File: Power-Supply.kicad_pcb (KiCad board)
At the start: 2 copper layers, 76 x 76.2 mm, 72 parts, among them J2 ADC1, J3 ADC2, J4 DAC1, J5 DAC2, J6 DAC3, J7 FPGA, J8 Frontpanel, J9 RPT-75C, U1 LT3081xR, U2 LT3081xR, U3 LT3091xR, U4 SIP10-05, U5 AMS1117-3.3, U6 DNT04

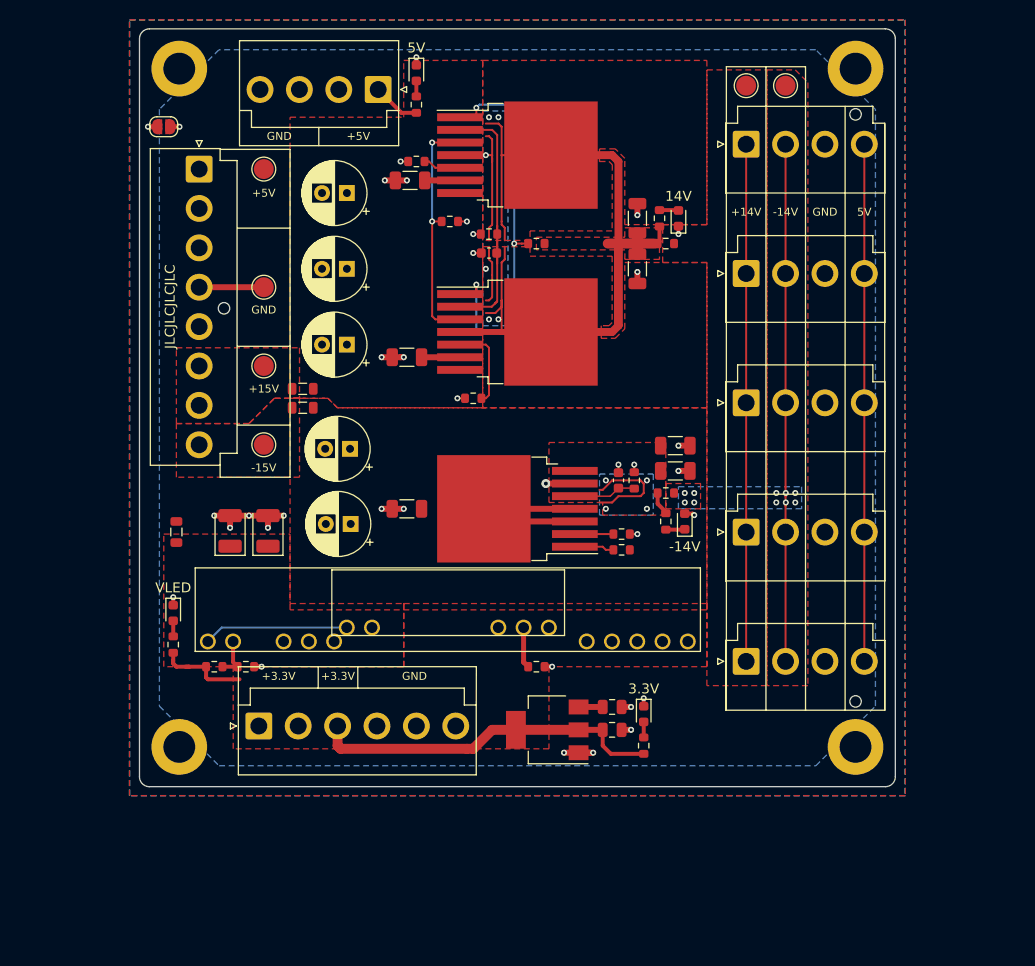
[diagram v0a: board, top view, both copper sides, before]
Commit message: Update to KiCad 6
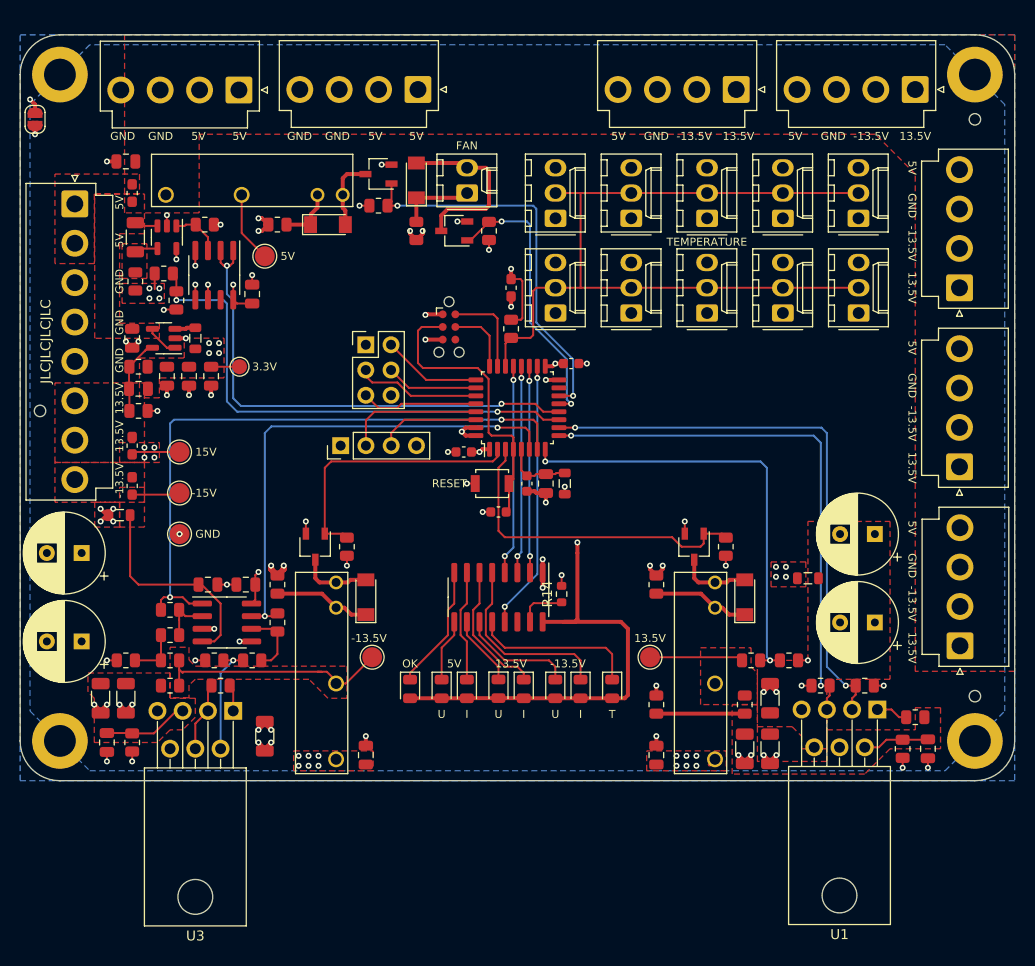
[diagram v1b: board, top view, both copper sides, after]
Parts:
- removed C10, C9: 10u, Capacitor_SMD:C_0805_2012Metric
- removed C11, C12: 100u, Capacitor_Tantalum_SMD:CP_EIA-3528-21_Kemet-B
- removed C13: 10u/50V, Capacitor_SMD:C_1206_3216Metric
- removed C18: 220u, Capacitor_THT:CP_Radial_D6.3mm_P2.50mm
- removed L1: 600R/100M, Inductor_SMD:L_0805_2012Metric
- removed R19, R20: NC, Resistor_SMD:R_0603_1608Metric
- removed R21: 3k, Resistor_SMD:R_0603_1608Metric
- removed U5: AMS1117-3.3, Package_TO_SOT_SMD:SOT-223-3_TabPin2
- removed U6: DNT04, twam-Misc:DNT04
- added C19: 100nF, Capacitor_SMD:C_0805_2012Metric, F.Cu at (164.0, 134.9)
- added C20: 100nF, Capacitor_SMD:C_0805_2012Metric, F.Cu at (134.8, 134.9)
- added C21: 100nF, Capacitor_SMD:C_0805_2012Metric, F.Cu at (122.7, 117.8)
- added C22: 100nF, Capacitor_SMD:C_0805_2012Metric, F.Cu at (118.9, 117.8)
- added C23: 4u7, Capacitor_SMD:C_0805_2012Metric, F.Cu at (111.3, 93.0)
- added C24: 10p, Capacitor_SMD:C_0805_2012Metric, F.Cu at (111.9, 98.1)
- added C25: 10u, Capacitor_SMD:C_0805_2012Metric, F.Cu at (114.8, 96.8)
- added C26: 10u, Capacitor_SMD:C_0805_2012Metric, F.Cu at (117.0, 96.8)
- added C27: 1u, Capacitor_SMD:C_0805_2012Metric, F.Cu at (119.2, 96.8)
- added C28: 100nF, Capacitor_SMD:C_0805_2012Metric, F.Cu at (110.6, 75.2)
- added C29: 100nF, Capacitor_SMD:C_0805_2012Metric, F.Cu at (123.3, 88.6)
- added C30: 100nF, Capacitor_SMD:C_0603_1608Metric, F.Cu at (148.1, 110.5)
- added C31: 100nF, Capacitor_SMD:C_0603_1608Metric, F.Cu at (144.6, 104.4)
- added C32: 100nF, Capacitor_SMD:C_0603_1608Metric, F.Cu at (155.4, 95.6)
- added C33: 100nF, Capacitor_SMD:C_0603_1608Metric, F.Cu at (151.0, 107.6)
- added C34: 10u, Capacitor_SMD:C_0805_2012Metric, F.Cu at (152.9, 107.6)
- added D10: red, LED_SMD:LED_0805_2012Metric, F.Cu at (156.3, 128.3)
- added D11: red, LED_SMD:LED_0805_2012Metric, F.Cu at (159.5, 128.3)
- added D12: LL4148, Diode_SMD:D_MiniMELF, F.Cu at (139.8, 77.1)
- added D6: red, LED_SMD:LED_0805_2012Metric, F.Cu at (144.9, 128.3)
- added D7: red, LED_SMD:LED_0805_2012Metric, F.Cu at (148.1, 128.3)
- added D8: red, LED_SMD:LED_0805_2012Metric, F.Cu at (150.6, 128.3)
- added D9: red, LED_SMD:LED_0805_2012Metric, F.Cu at (153.8, 128.3)
- added F1: 2A, Fuse:Fuse_0603_1608Metric_Pad1.05x0.95mm_HandSolder, F.Cu at (111.3, 78.4)
- added F2: 2A, Fuse:Fuse_0603_1608Metric_Pad1.05x0.95mm_HandSolder, F.Cu at (111.3, 107.9)
- added F3: 2A, Fuse:Fuse_0603_1608Metric_Pad1.05x0.95mm_HandSolder, F.Cu at (111.3, 103.8)
- added F4: 50mA, Fuse:Fuse_0603_1608Metric_Pad1.05x0.95mm_HandSolder, F.Cu at (149.4, 87.9)
- added J1: SWD, Connector:Tag-Connect_TC2030-IDC-NL_2x03_P1.27mm_Vertical, F.Cu at (143.1, 91.9)
- added J10: TEMP, Connector_Molex:Molex_KK-254_AE-6410-03A_1x03_P2.54mm_Vertical, F.Cu at (176.7, 81.0)
- added J11: TEMP, Connector_Molex:Molex_KK-254_AE-6410-03A_1x03_P2.54mm_Vertical, F.Cu at (169.1, 81.0)
- added J12: TEMP, Connector_Molex:Molex_KK-254_AE-6410-03A_1x03_P2.54mm_Vertical, F.Cu at (184.3, 81.0)
- added J13: TEMP, Connector_Molex:Molex_KK-254_AE-6410-03A_1x03_P2.54mm_Vertical, F.Cu at (176.7, 90.5)
- added J14: TEMP, Connector_Molex:Molex_KK-254_AE-6410-03A_1x03_P2.54mm_Vertical, F.Cu at (161.4, 90.5)
- added J15: TEMP, Connector_Molex:Molex_KK-254_AE-6410-03A_1x03_P2.54mm_Vertical, F.Cu at (161.4, 81.0)
- added J16: TEMP, Connector_Molex:Molex_KK-254_AE-6410-03A_1x03_P2.54mm_Vertical, F.Cu at (184.3, 90.5)
- added J17: TEMP, Connector_Molex:Molex_KK-254_AE-6410-03A_1x03_P2.54mm_Vertical, F.Cu at (153.8, 81.0)
- added J18: SPI, Connector_PinHeader_2.54mm:PinHeader_2x03_P2.54mm_Vertical, F.Cu at (134.8, 93.7)
- added J19: TEMP, Connector_Molex:Molex_KK-254_AE-6410-03A_1x03_P2.54mm_Vertical, F.Cu at (153.8, 90.5)
- added J20: TEMP, Connector_Molex:Molex_KK-254_AE-6410-03A_1x03_P2.54mm_Vertical, F.Cu at (169.1, 90.5)
- added J21: FAN, Connector_Molex:Molex_KK-254_AE-6410-02A_1x02_P2.54mm_Vertical, F.Cu at (144.9, 78.4)
- added J22: UART, Connector_PinHeader_2.54mm:PinHeader_1x04_P2.54mm_Vertical, F.Cu at (132.2, 103.8)
- added K1: PCN1xxx3MHZ,xxx, twam-Misc:PCN1xxx3MHZ,xxx, F.Cu at (169.9, 135.3)
- added K2: PCN1xxx3MHZ,xxx, twam-Misc:PCN1xxx3MHZ,xxx, F.Cu at (131.8, 135.3)
- added K3: PCN1xxx3MHZ,xxx, twam-Misc:PCN1xxx3MHZ,xxx, F.Cu at (114.7, 78.6)
- added L4: 2u2, Inductor_SMD:L_0805_2012Metric, F.Cu at (117.6, 93.0)
- added L5: 600R/100M, Inductor_SMD:L_0805_2012Metric, F.Cu at (154.8, 107.6)
- added Q1: AO3400A, Package_TO_SOT_SMD:TSOT-23, F.Cu at (167.8, 114.0)
- added Q2: AO3400A, Package_TO_SOT_SMD:TSOT-23, F.Cu at (129.7, 114.0)
- added Q3: AO3400A, Package_TO_SOT_SMD:TSOT-23, F.Cu at (136.0, 76.5)
- added Q4: AO3400A, Package_TO_SOT_SMD:TSOT-23, F.Cu at (143.7, 82.2)
- added R15: 0R, Resistor_SMD:R_0805_2012Metric, F.Cu at (164.0, 117.8)
- added R16: 10k, Resistor_SMD:R_0805_2012Metric, F.Cu at (171.0, 114.0)
- added R18: 11k, Resistor_SMD:R_0805_2012Metric, F.Cu at (110.6, 125.4)
- added R22: 0R, Resistor_SMD:R_0805_2012Metric, F.Cu at (125.9, 117.8)
- added R23: 10k, Resistor_SMD:R_0805_2012Metric, F.Cu at (132.9, 114.0)
- added R25: 11k, Resistor_SMD:R_0805_2012Metric, F.Cu at (115.1, 122.9)
- added R26: 0R, Resistor_SMD:R_0805_2012Metric, F.Cu at (123.3, 125.4)
- added R27: 11k, Resistor_SMD:R_0805_2012Metric, F.Cu at (115.1, 120.3)
- added R28: 10k, Resistor_SMD:R_0805_2012Metric, F.Cu at (125.9, 121.6)
- added R29: 0R01, Resistor_SMD:R_1206_3216Metric, F.Cu at (111.6, 82.9)
- added R30: 249k, Resistor_SMD:R_0805_2012Metric, F.Cu at (118.6, 81.6)
- added R31: 0R, Resistor_SMD:R_0805_2012Metric, F.Cu at (111.6, 87.3)
- added R32: 10k, Resistor_SMD:R_0805_2012Metric, F.Cu at (114.4, 86.5)
- added R33: 10k, Resistor_SMD:R_0805_2012Metric, F.Cu at (115.7, 89.2)
- added R34: 0R, Resistor_SMD:R_0805_2012Metric, F.Cu at (125.9, 81.6)
- added R35: 10k, Resistor_SMD:R_0805_2012Metric, F.Cu at (136.0, 79.7)
- added R36: 10k, Resistor_SMD:R_0805_2012Metric, F.Cu at (149.4, 92.1)
- added R38: 10k, Resistor_SMD:R_0805_2012Metric, F.Cu at (147.1, 82.2)
- added R39: 81R, Resistor_SMD:R_0805_2012Metric, F.Cu at (139.8, 82.2)
- added R9: 39k, Resistor_SMD:R_0805_2012Metric, F.Cu at (173.5, 125.4)
- added SW1: RESET, Button_Switch_SMD:SW_SPST_B3U-1000P, F.Cu at (147.5, 107.6)
- added TP7: 5V, TestPoint:TestPoint_Pad_D2.0mm, F.Cu at (124.6, 84.8)
- added U10: MCP6002-xSN, Package_SO:SOIC-8_3.9x4.9mm_P1.27mm, F.Cu at (119.5, 86.7)
- added U7: NE5532, Package_SO:SOIC-8_3.9x4.9mm_P1.27mm, F.Cu at (120.8, 121.6)
- added U8: TLV62569DBV, Package_TO_SOT_SMD:SOT-23-5, F.Cu at (114.4, 93.0)
- added U9: INA138, Package_TO_SOT_SMD:SOT-23-5, F.Cu at (114.8, 82.9)
- C14, C15, C16, C17: value 220u -> 220u/35V; footprint Capacitor_THT:CP_Radial_D6.3mm_P2.50mm -> Capacitor_THT:CP_Radial_D8.0mm_P3.50mm
- C4, C8: value 20pF -> 100nF; footprint Capacitor_SMD:C_0603_1608Metric -> Capacitor_SMD:C_0805_2012Metric
- D1, D2, D3: value green -> LL4148; footprint LED_SMD:LED_0603_1608Metric -> Diode_SMD:D_MiniMELF
- D4: footprint LED_SMD:LED_0603_1608Metric -> LED_SMD:LED_0805_2012Metric
- D5: value green -> red; footprint LED_SMD:LED_0603_1608Metric -> LED_SMD:LED_0805_2012Metric
- J8: footprint Connector_JST:JST_VH_B6P-VH_1x06_P3.96mm_Vertical -> Connector_JST:JST_VH_B4P-VH_1x04_P3.96mm_Vertical
- R1, R24, R3, R7, R8: footprint Resistor_SMD:R_0603_1608Metric -> Resistor_SMD:R_0805_2012Metric
- R10: value 3k9 -> 4k7; footprint Resistor_SMD:R_0603_1608Metric -> Resistor_SMD:R_0805_2012Metric
- R11: value 68k -> 11k; footprint Resistor_SMD:R_0603_1608Metric -> Resistor_SMD:R_0805_2012Metric
- R12: value 68k -> 39k; footprint Resistor_SMD:R_0603_1608Metric -> Resistor_SMD:R_0805_2012Metric
- R13: value 4k7 -> 68k; footprint Resistor_SMD:R_0603_1608Metric -> Resistor_SMD:R_0805_2012Metric
- R14: value 4k7 -> 470R
- R17: value 280k -> 270k; footprint Resistor_SMD:R_0603_1608Metric -> Resistor_SMD:R_0805_2012Metric
- R2: value 6k8 -> 2k; footprint Resistor_SMD:R_0603_1608Metric -> Resistor_SMD:R_0805_2012Metric
- R4: value 140k -> 270k; footprint Resistor_SMD:R_0603_1608Metric -> Resistor_SMD:R_0805_2012Metric
- R5: value 22k -> 3k3; footprint Resistor_SMD:R_0603_1608Metric -> Resistor_SMD:R_0805_2012Metric
- R6: value 3k9 -> 11k; footprint Resistor_SMD:R_0603_1608Metric -> Resistor_SMD:R_0805_2012Metric
- TP2: value 14V -> 13.5V
- TP3: value 5V -> 3V3; footprint TestPoint:TestPoint_Pad_D2.0mm -> TestPoint:TestPoint_Pad_D1.5mm
- TP6: value -14V -> -13.5V
- U1, U3: footprint Package_TO_SOT_SMD:TO-263-7_TabPin4 -> Package_TO_SOT_THT:TO-220-7_P2.54x3.8mm_StaggerOdd_Lead5.85mm_TabDown
- U2: value LT3081xR -> STM32L051K8Tx; footprint Package_TO_SOT_SMD:TO-263-7_TabPin4 -> Package_QFP:LQFP-32_7x7mm_P0.8mm
- U4: value SIP10-05 -> TLC5916IDR; footprint twam-Misc:SIP10-05 -> Package_SO:SOIC-16_3.9x9.9mm_P1.27mm
- moved H6 87.3 mm to (102.0, 100.3)
- moved H5 77.9 mm to (196.0, 71.0)
- moved TP6 70.9 mm to (135.4, 125.1)
- moved C15 68.4 mm to (185.9, 121.6)
- moved C4 66.6 mm to (191.3, 134.3), turned to 90 degrees
- moved R3 66.6 mm to (180.5, 127.9)
- moved U1 66.5 mm to (186.2, 130.3), turned to 180 degrees
- moved R4 66.4 mm to (188.7, 134.3), turned to 90 degrees
- moved J8 66.0 mm to (140.0, 68.0), turned to 180 degrees
- moved R6 62.6 mm to (184.9, 127.9)
- moved C6 62.1 mm to (108.1, 129.2), turned to -90 degrees
- moved D5 62.0 mm to (142.4, 128.3)
- moved R2 61.0 mm to (190.0, 131.1)
- moved C5 60.8 mm to (110.6, 129.2), turned to -90 degrees
- moved TP2 58.3 mm to (163.3, 125.1)
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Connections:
- net /-14V_IN renamed /Negative Supply/-13V5_IN
- net Net-(R10-Pad1) renamed /Negative Supply/~{ADC_I_-13V5}
- C1 pad 1: /14V_OUT -> /Positive Supply/13V5_OUT
- C14 pad 1: /14V_IN -> /Positive Supply/13V5_IN
- C15 pad 1: /14V_IN -> /Positive Supply/13V5_IN
- C2 pad 1: /14V_OUT -> /Positive Supply/13V5_OUT
- C3 pad 2: /14V_IN -> /Positive Supply/13V5_IN
- C5 pad 1: /-14V_OUT -> /Negative Supply/-13V5_OUT
- C6 pad 1: /-14V_OUT -> /Negative Supply/-13V5_OUT
- D1 pad 1: GND -> Net-(D1-Pad1)
- D2 pad 2: GND -> Net-(D2-Pad2)
- D3 pad 1: GND -> Net-(D3-Pad1)
- D4 pad 1: GND -> Net-(D4-Pad1)
- D4 pad 2: Net-(D4-Pad2) -> /Digital Supply/3V3
- D5 pad 1: GND -> Net-(D5-Pad1)
- D5 pad 2: Net-(D5-Pad2) -> /Digital Supply/3V3
- J2 pad 1: /14V -> /Positive Supply/13V5
- J2 pad 2: /-14V -> /Negative Supply/-13V5
- J2 pad 4: /5V -> /Digital Supply/5V0
- J3 pad 1: /14V -> /Positive Supply/13V5
- J3 pad 2: /-14V -> /Negative Supply/-13V5
- J3 pad 4: /5V -> /Digital Supply/5V0
- J4 pad 1: /14V -> /Positive Supply/13V5
- J4 pad 2: /-14V -> /Negative Supply/-13V5
- J4 pad 4: /5V -> /Digital Supply/5V0
- J5 pad 1: /14V -> /Positive Supply/13V5
- J5 pad 2: /-14V -> /Negative Supply/-13V5
- J5 pad 4: /5V -> /Digital Supply/5V0
- J6 pad 1: /14V -> /Positive Supply/13V5
- J6 pad 2: /-14V -> /Negative Supply/-13V5
- J6 pad 4: /5V -> /Digital Supply/5V0
- J7 pad 1: /5V -> /Digital Supply/5V0
- J7 pad 2: /5V -> /Digital Supply/5V0
- J8 pad 1: /VLED -> /Digital Supply/5V0
- J8 pad 2: /VLED -> /Digital Supply/5V0
- J8 pad 3: /3V3_FRONT -> GND
- J9 pad 1: /5V -> Net-(F1-Pad2)
- J9 pad 2: /5V -> Net-(F1-Pad2)
- J9 pad 6: /15V -> Net-(F3-Pad2)
- J9 pad 7: /15V -> Net-(F3-Pad2)
- J9 pad 8: /-15V -> Net-(F2-Pad2)
- L2 pad 1: /15V -> /Digital Supply/15V
- L2 pad 2: /14V_IN -> /Positive Supply/13V5_IN
- L3 pad 1: /-15V -> /Negative Supply/-15V
- R1 pad 1: /14V -> /Positive Supply/13V5_PRE_RELAIS
- R1 pad 2: /14V_OUT -> /Positive Supply/13V5_OUT
- R11 pad 1: /14V_OUT -> /Microcontroller/ADC_U_13V5
- R11 pad 2: Net-(D1-Pad2) -> GND
- R12 pad 1: /-14V_OUT -> /Negative Supply/-13V5_PRE_RELAIS
- R12 pad 2: Net-(D2-Pad1) -> /Negative Supply/~{ADC_U_-13V5}
- R13 pad 1: /VLED -> /Digital Supply/3V3
- R13 pad 2: Net-(D3-Pad2) -> Net-(C24-Pad2)
- R14 pad 1: /3V3_FRONT -> Net-(R14-Pad1)
- R14 pad 2: Net-(D4-Pad2) -> GND
- R2 pad 1: /14V_OUT -> /Positive Supply/13V5_OUT
- R24 pad 1: /5V -> Net-(C24-Pad2)
- R24 pad 2: Net-(D5-Pad2) -> GND
- R3 pad 2: Net-(R3-Pad2) -> /Microcontroller/ADC_T_13V5
- R5 pad 1: GND -> /Positive Supply/13V5_OUT
- R5 pad 2: Net-(R5-Pad2) -> GND
- R6 pad 1: Net-(R6-Pad1) -> /Microcontroller/ADC_I_13V5
- R7 pad 1: /-14V -> /Negative Supply/-13V5_PRE_RELAIS
- R7 pad 2: /-14V_OUT -> /Negative Supply/-13V5_OUT
- TP1 pad 1: /15V -> /Digital Supply/15V
- TP2 pad 1: /14V -> /Positive Supply/13V5_PRE_RELAIS
- TP3 pad 1: /5V -> /Digital Supply/3V3
- TP5 pad 1: /-15V -> /Negative Supply/-15V
- TP6 pad 1: /-14V -> /Negative Supply/-13V5_PRE_RELAIS
- U1 pad 3: Net-(R6-Pad1) -> /Microcontroller/ADC_I_13V5
- U1 pad 4: /14V_OUT -> /Positive Supply/13V5_OUT
- U1 pad 5: Net-(R3-Pad2) -> /Microcontroller/ADC_T_13V5
- U1 pad 6: /14V_IN -> /Positive Supply/13V5_IN
- U1 pad 7: Net-(U1-Pad7) -> unconnected-(U1-Pad7)
- U2 pad 1: Net-(R2-Pad2) -> /Digital Supply/3V3
- U2 pad 2: Net-(C4-Pad2) -> /Microcontroller/ENABLE_-13V5
- U2 pad 3: Net-(R6-Pad1) -> /Microcontroller/ENABLE_13V5
- U2 pad 4: /14V_OUT -> /Microcontroller/~{RESET}
- U2 pad 5: Net-(R5-Pad2) -> /Microcontroller/3V3A
- U2 pad 6: /14V_IN -> /Microcontroller/ADC_I_-13V5
- U2 pad 7: Net-(U2-Pad7) -> /Microcontroller/ADC_U_-13V5
- U3 pad 7: /-14V_OUT -> /Negative Supply/-13V5_OUT
- U4 pad 1: /VLED -> GND
- U4 pad 11: /VLED_ONOFF -> Net-(D9-Pad1)
- U4 pad 2: /VLED -> /Microcontroller/LED_SDI
- U4 pad 3: /VLED -> /Microcontroller/LED_CLK
- U4 pad 4: /VLED -> /Microcontroller/LED_LE
- U4 pad 5: GND -> Net-(D10-Pad1)
- U4 pad 6: GND -> Net-(D8-Pad1)
- U4 pad 7: /VLED_5V -> Net-(D6-Pad1)
- U4 pad 8: /VLED_5V -> Net-(D4-Pad1)
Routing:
- net /14V_OUT: track 126.8 -> 0.00 mm, vias 6 -> 0
- net /Microcontroller/ONEWIRE: track 0.00 -> 82.7 mm
- net /Digital Supply/3V3: track 0.00 -> 62.9 mm, vias 0 -> 13
- net /Microcontroller/ADC_U_-13V5: track 0.00 -> 62.8 mm, vias 0 -> 2
- net /5V: track 59.8 -> 0.00 mm
- net /Microcontroller/ADC_I_13V5: track 0.00 -> 56.9 mm, vias 0 -> 2
- net /Microcontroller/ADC_T_13V5: track 0.00 -> 54.5 mm, vias 0 -> 2
- net /Digital Supply/ADC_U_5V0: track 0.00 -> 52.0 mm, vias 0 -> 2
- net /14V: track 52.0 -> 0.00 mm
- net /-14V: track 52.0 -> 0.00 mm, vias 10 -> 0
- net /Digital Supply/ADC_I_5V0: track 0.00 -> 51.0 mm, vias 0 -> 2
- net /Microcontroller/ADC_I_-13V5: track 0.00 -> 50.0 mm, vias 0 -> 2
- net /Microcontroller/ADC_U_13V5: track 0.00 -> 45.3 mm, vias 0 -> 2
- net /Digital Supply/ENABLE_5V0: track 0.00 -> 39.2 mm, vias 0 -> 2
- net Net-(R2-Pad2): track 41.0 -> 3.56 mm, vias 3 -> 0
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- added copper zone on F.Cu, net /Digital Supply/15V
- added copper zone on In2.Cu, net /Digital Supply/15V
- added copper zone on F.Cu, net /Digital Supply/3V3
- added copper zone on In2.Cu, net /Digital Supply/3V3
- added copper zone on F.Cu, net /Digital Supply/5V
- added copper zone on F.Cu, net /Digital Supply/5V0
- added copper zone on F.Cu, net /Negative Supply/-13V5
- added copper zone on In2.Cu, net /Negative Supply/-13V5
- added copper zone on In2.Cu, net /Negative Supply/-13V5_IN
- added copper zone on F.Cu, net /Negative Supply/-13V5_OUT
- added copper zone on In1.Cu, net /Negative Supply/-13V5_OUT
- added copper zone on F.Cu, net /Negative Supply/-13V5_PRE_RELAIS
- added copper zone on F.Cu, net /Negative Supply/-15V
- added copper zone on F.Cu, net /Positive Supply/13V5
- added copper zone on In2.Cu, net /Positive Supply/13V5
- added copper zone on F.Cu, net /Positive Supply/13V5_IN
- added copper zone on F.Cu, net /Positive Supply/13V5_OUT
- added copper zone on In1.Cu, net /Positive Supply/13V5_OUT
- added copper zone on F.Cu, net /Positive Supply/13V5_PRE_RELAIS
- added copper zone on In1.Cu, net GND
- added copper zone on F.Cu, net Net-(F1-Pad2)
- added copper zone on F.Cu, net Net-(F2-Pad2)
- added copper zone on F.Cu, net Net-(F3-Pad2)
- added copper zone on In2.Cu, net Net-(F4-Pad1)
- added copper zone on F.Cu, net Net-(K3-Pad14)
- added copper zone on In2.Cu, net Net-(K3-Pad14)
- added copper zone on F.Cu, net Net-(R29-Pad1)
- removed copper zone on B.Cu, net /-14V
- removed copper zone on F.Cu, net /-14V
- removed copper zone on B.Cu, net /-14V_OUT
- removed copper zone on F.Cu, net /-14V_OUT
- removed copper zone on F.Cu, net /-15V
- removed copper zone on F.Cu, net /14V
- removed copper zone on F.Cu, net /14V_IN
- removed copper zone on B.Cu, net /14V_OUT
- removed copper zone on F.Cu, net /14V_OUT
- removed copper zone on F.Cu, net /15V
- removed copper zone on F.Cu, net /5V
- removed copper zone on F.Cu, net /VLED
- removed copper zone on F.Cu, net /VLED_5V
- removed copper zone on B.Cu, net GND
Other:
- board size 76 x 76.2 mm -> 100 x 75 mm
- copper layers 2 -> 4
- rule pad_to_mask_clearance: 0 -> 0.05
- rule solder_mask_min_width: 0.12 -> 0.2
- board text added: "-13.5V"
- board text added: "13.5V"
- board text added: "15V"
- board text added: "FAN"
- board text added: "I"
- board text added: "OK"
- board text added: "Power Supply Rev. 3, 2021-06-14 Tobias Müller, twam.info"
- board text added: "RESET"
- board text added: "T"
- board text added: "TEMPERATURE"
- board text added: "U"
- board text removed: "+14V"
- board text removed: "+15V"
- board text removed: "+3.3V"
- board text removed: "+5V"
- board text removed: "-14V"
- board text removed: "14V"
- board text removed: "Power Supply Rev. 2, 2021-03-22 Tobias Müller, twam.info"
- board text removed: "VLED"
